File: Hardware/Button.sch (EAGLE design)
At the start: 39 parts, among them IC1 STM32F030C6T, IC2 MCP73831, M2 WIRELESS-NRF24L01, Q1 IRLML5203, Q2 BC817-16LT1SMD, Q3 BC817-16LT1SMD, X1 MINI-USB-UX60-MB-5ST

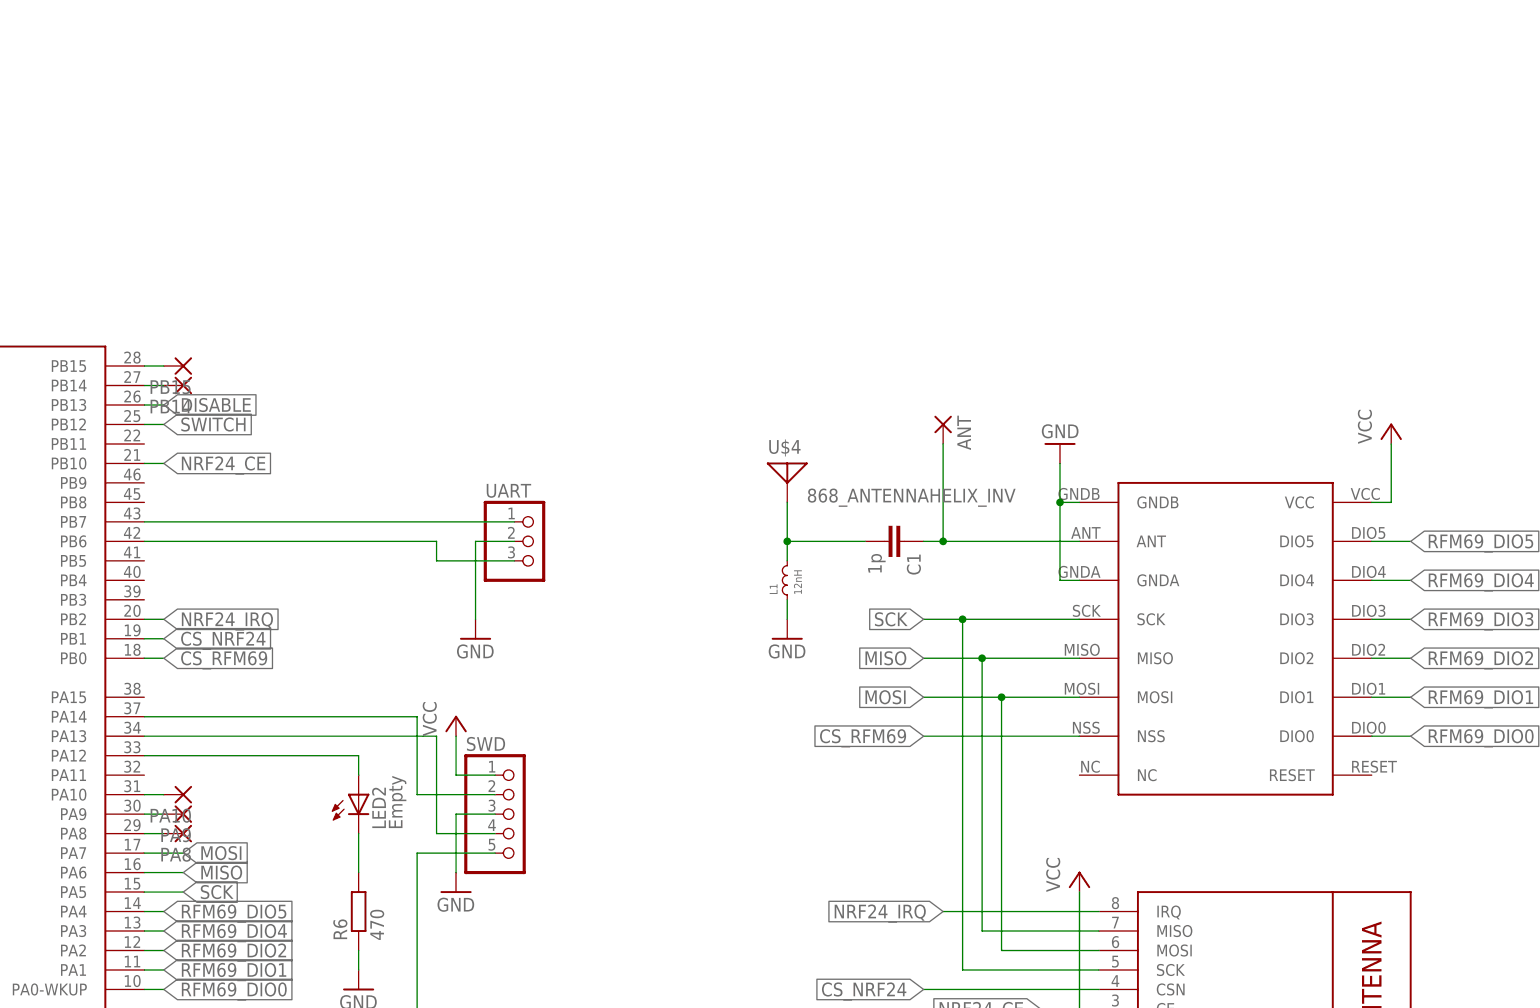
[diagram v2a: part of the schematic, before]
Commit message: LED output added to button
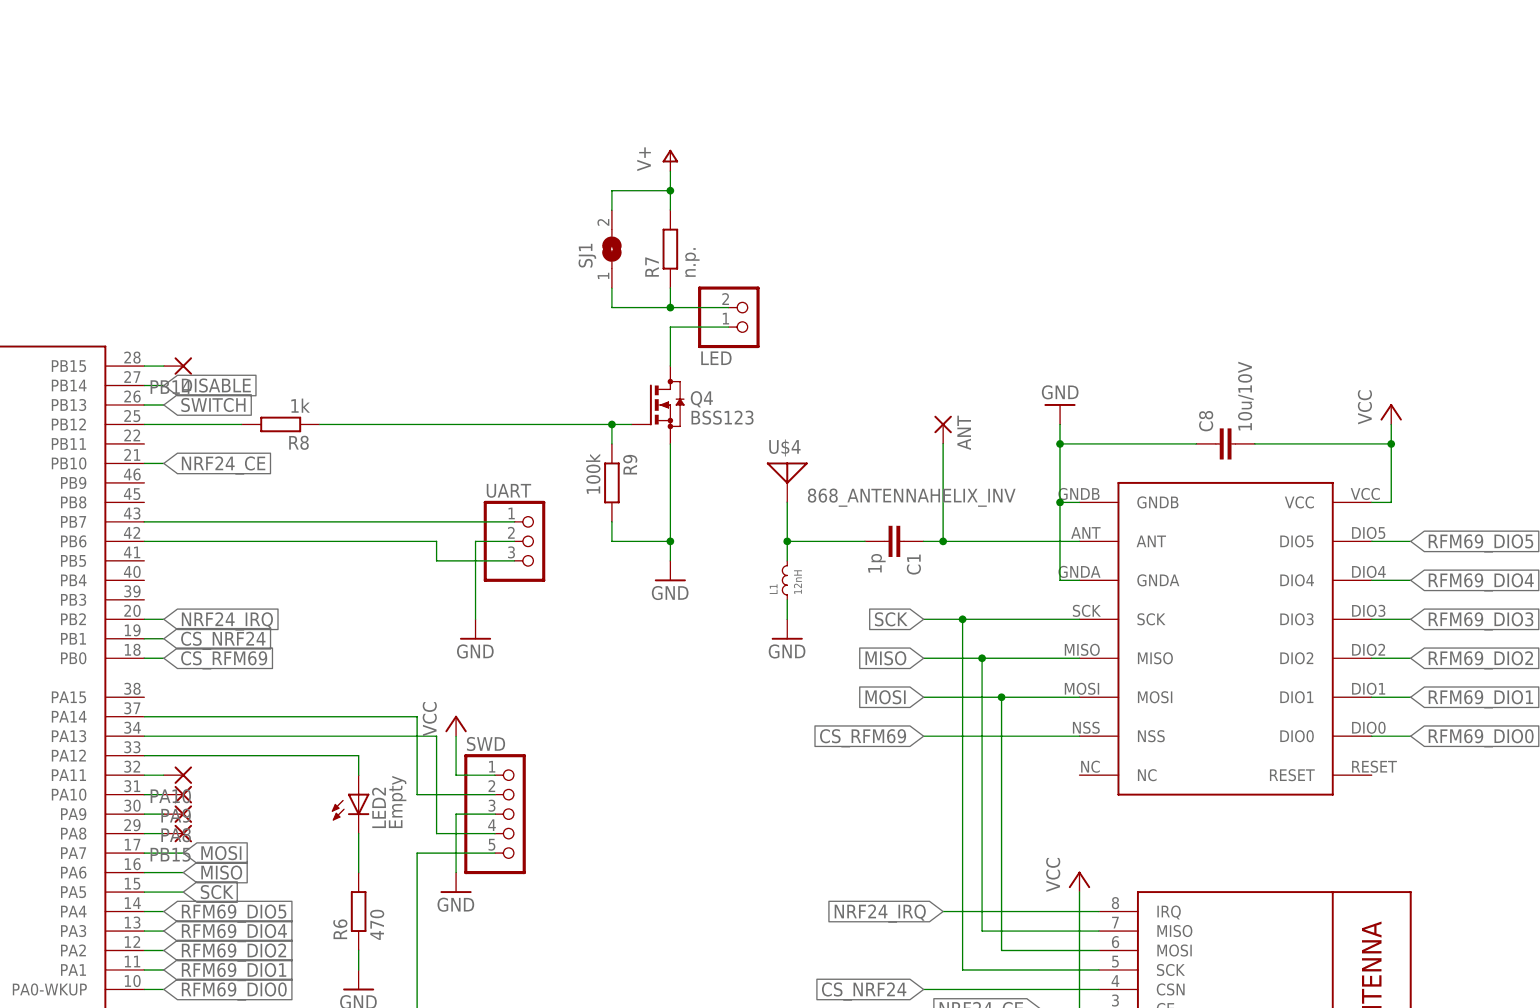
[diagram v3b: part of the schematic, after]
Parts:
- added C8: 10u/10V, rcl:C-EUC1206
- added LED: (no value), pinhead:PINHD-1X2
- added Q4: BSS123, transistor-small-signal:BSS123
- added R7: n.p., rcl:R-EU_R1206
- added R8: 1k, rcl:R-EU_R0603
- added R9: 100k, rcl:R-EU_R0603
- added SJ1: (no value), jumper:SJ
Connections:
- new net N$13: LED.1, Q4.D
- new net N$17: LED.2, R7.1, SJ1.1
- new net N$18: Q4.G, R8.1, R9.1
- new net N$19: IC1MCU.PB12, R8.2
- net DISABLE: now also IC1MCU.PB14; no longer IC1MCU.PB13
- net GND: now also C8.1, Q4.S, R9.2
- net N$11: now also IC1MCU.PA8; no longer IC1MCU.PB15
- net N$12: now also IC1MCU.PB15; no longer IC1MCU.PB14
- net N$14: now also IC1MCU.PA11; no longer IC1MCU.PA10
- net N$15: now also IC1MCU.PA10; no longer IC1MCU.PA9
- net N$16: now also IC1MCU.PA9; no longer IC1MCU.PA8
- net SWITCH: now also IC1MCU.PB13; no longer IC1MCU.PB12
- net V+: now also R7.2, SJ1.2
- net VCC: now also C8.2
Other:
- moved on the sheet: PA10, PA8, PA9, PB14, PB15

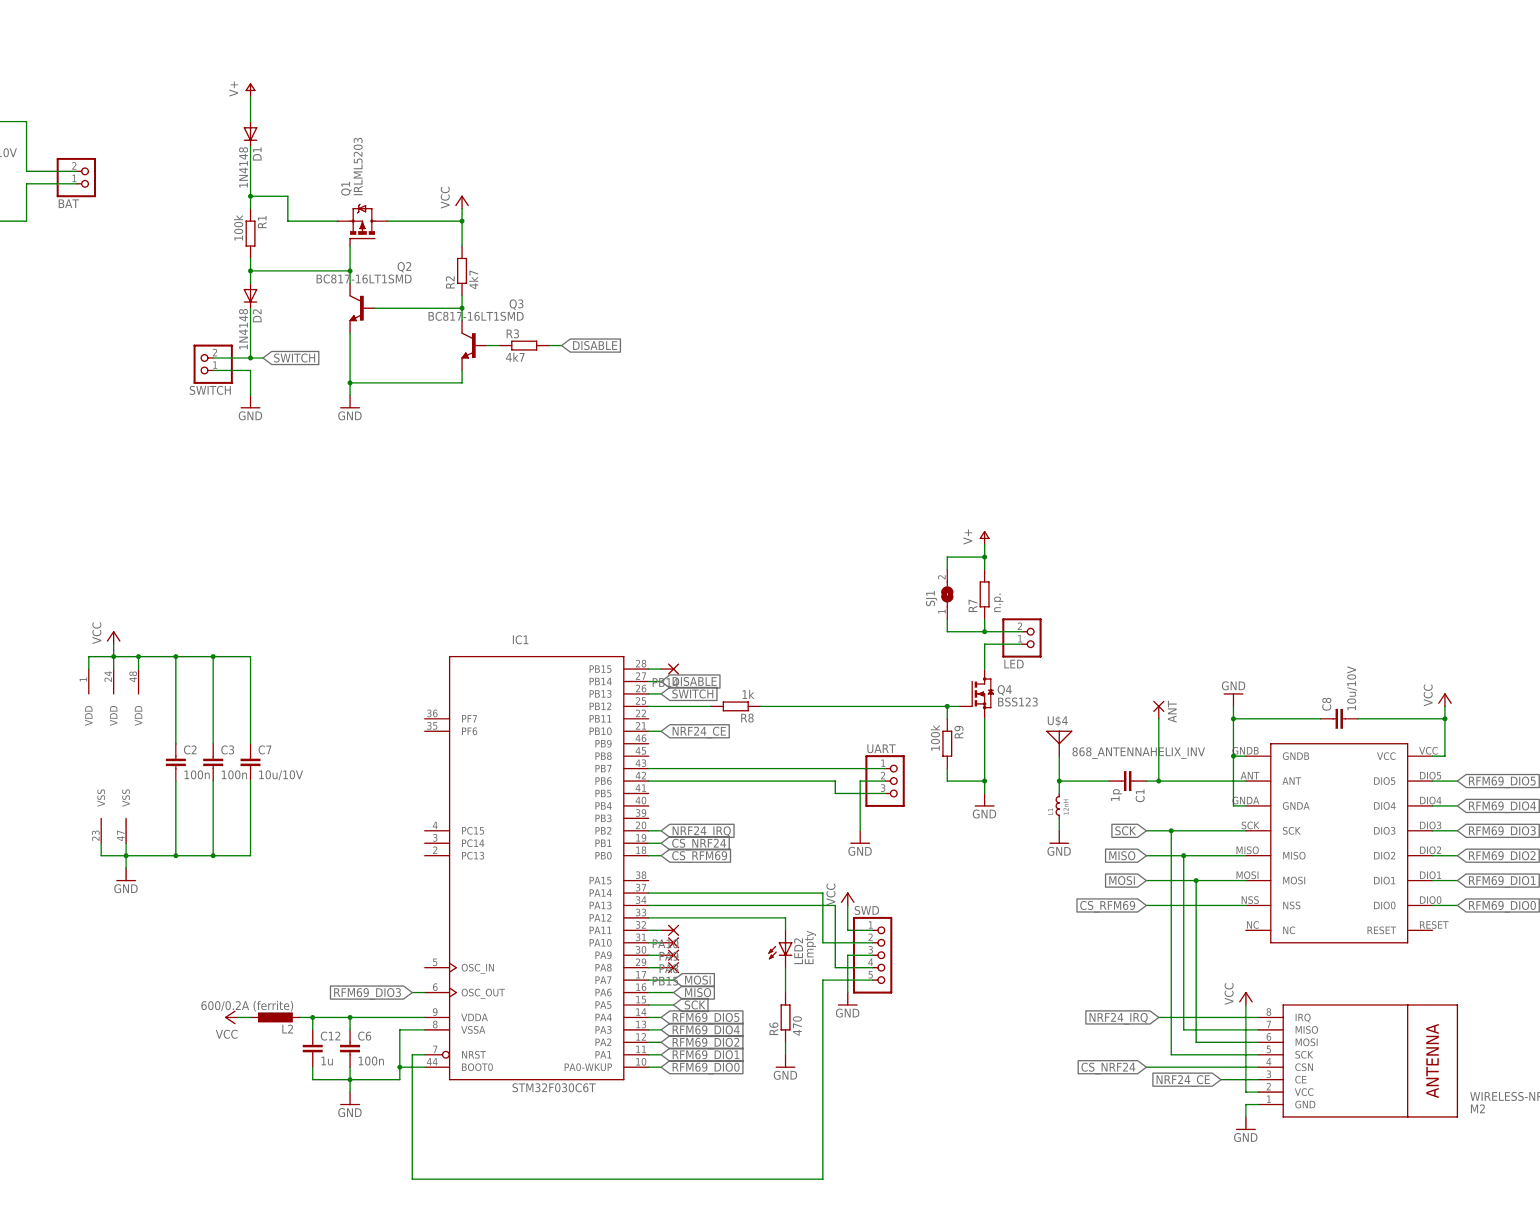
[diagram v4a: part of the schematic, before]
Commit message: 3V LDO + voltage sensing
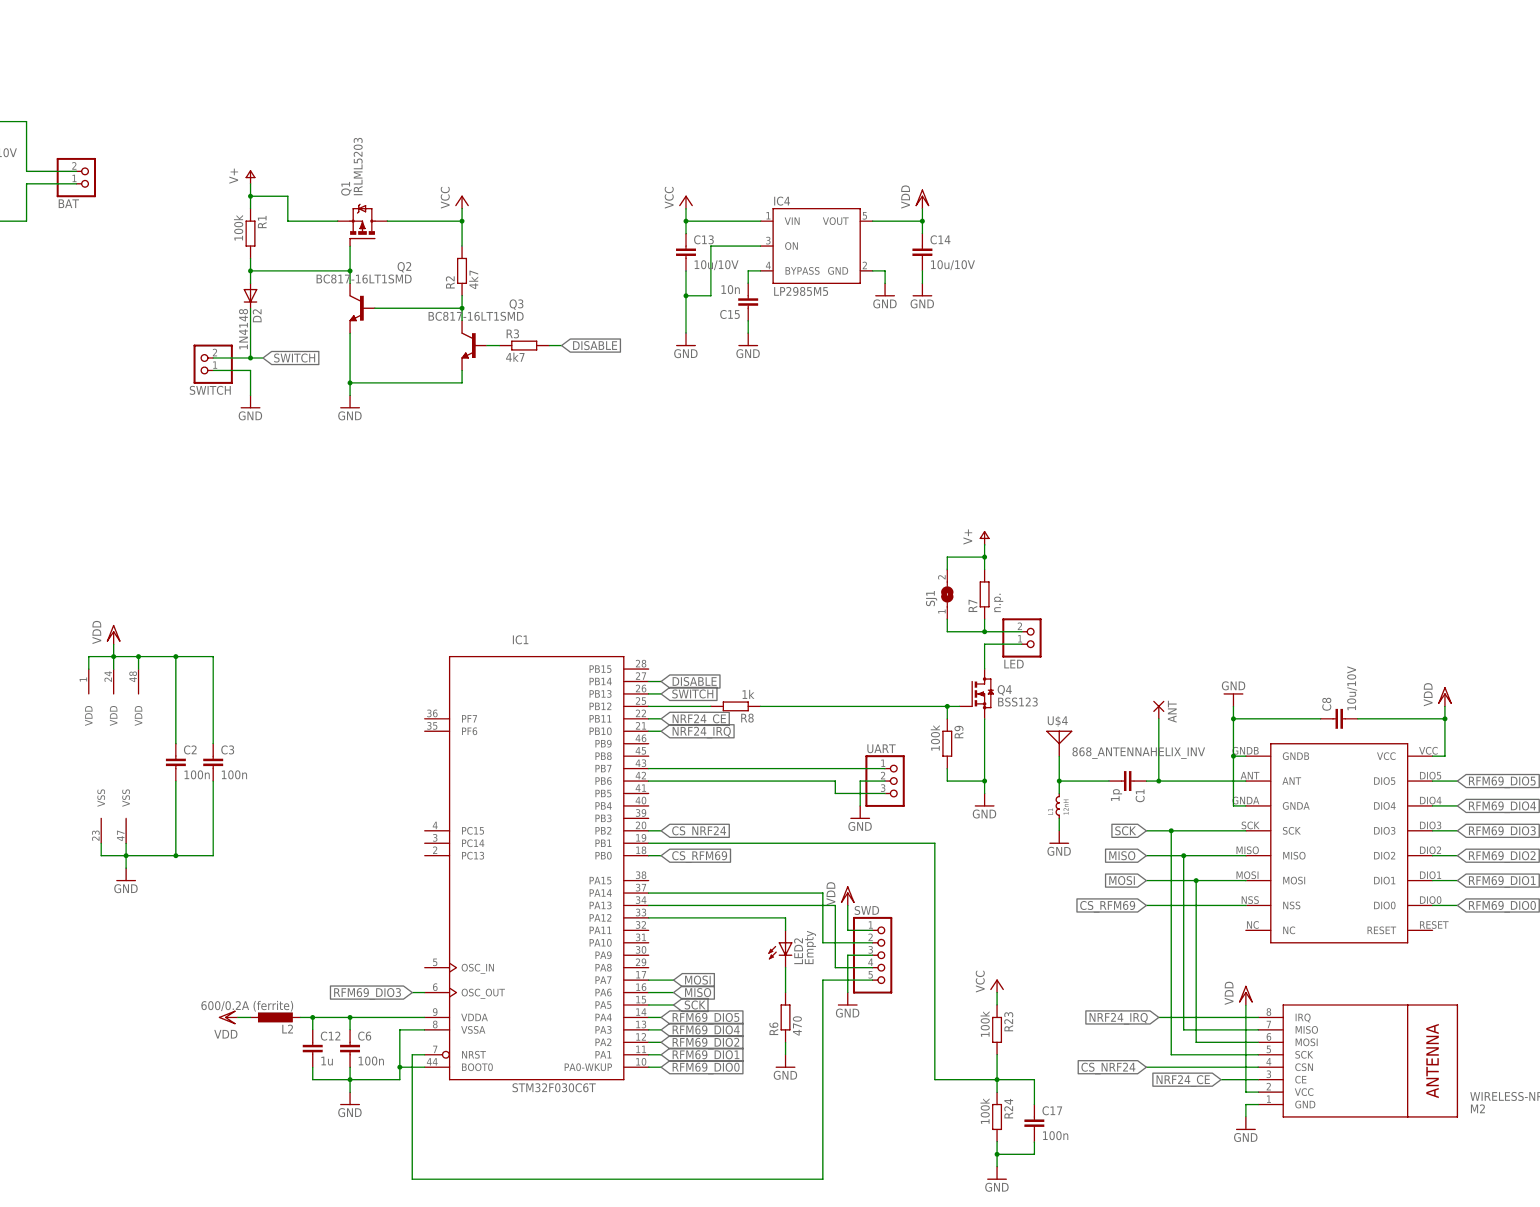
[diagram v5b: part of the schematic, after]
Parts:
- removed C7: 10u/10V, rcl:C-EUC1206
- removed D1: 1N4148, diode:DIODE-SOD323-W
- removed PA10, PA8, PA9, PB14, PB15: (no value), wirepad:SMD2
- added C13, C14: 10u/10V, rcl:C-EUC1206
- added C15: 10n, rcl:C-EUC0603
- added C17: 100n, rcl:C-EUC0603
- added IC4: LP2985M5, v-reg-3:LP2985M5
- added R23, R24: 100k, rcl:R-EU_R0603
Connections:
- removed net N$11: IC1MCU.PA8, PB15.P
- removed net N$12: IC1MCU.PB15, PB14.P
- removed net N$14: IC1MCU.PA11, PA10.P
- removed net N$15: IC1MCU.PA10, PA9.P
- removed net N$16: IC1MCU.PA9, PA8.P
- removed net N$6: D1.C, Q1.S, R1.1
- new net N$30: C15.2, IC4.BYPASS
- new net N$31: C17.1, IC1MCU.PB1, R23.2, R24.1
- new net VDD: C14.1, C2.1, C3.1, C8.2, IC1PWR.VDD@1, IC1PWR.VDD@2, IC1PWR.VDD@3, IC4.VOUT, L2.1, M2.VCC, SWD.1, U$1.VCC
- net CS_NRF24: now also IC1MCU.PB2; no longer IC1MCU.PB1
- net GND: now also C13.2, C14.2, C15.1, C17.2, IC4.GND, IC4.ON, R24.2; no longer C7.2
- net NRF24_CE: now also IC1MCU.PB11; no longer IC1MCU.PB10
- net NRF24_IRQ: now also IC1MCU.PB10; no longer IC1MCU.PB2
- net V+: now also Q1.S, R1.1; no longer D1.A
- net VCC: now also C13.1, IC4.VIN, R23.1; no longer C2.1, C3.1, C7.1, C8.2, IC1PWR.VDD@1, IC1PWR.VDD@2, IC1PWR.VDD@3, L2.1, M2.VCC, SWD.1, U$1.VCC
